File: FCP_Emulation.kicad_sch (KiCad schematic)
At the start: 115 parts, among them J1 Conn_01x10_Female, J2 Conn_01x10_Female, J3 Conn_01x10_Female, J4 Conn_01x02_Female, J5 Conn_01x02_Female, SW1 SW_DIP_x08, SW2 SW_DIP_x08, SW3 SW_DIP_x08, SW4 SW_DIP_x08, U1 LM2902, U2 LM2902, U3 LM2902, U4 LM2902, U5 LM2902, U6 LM2902, U7 LM2902, U8 LM2902

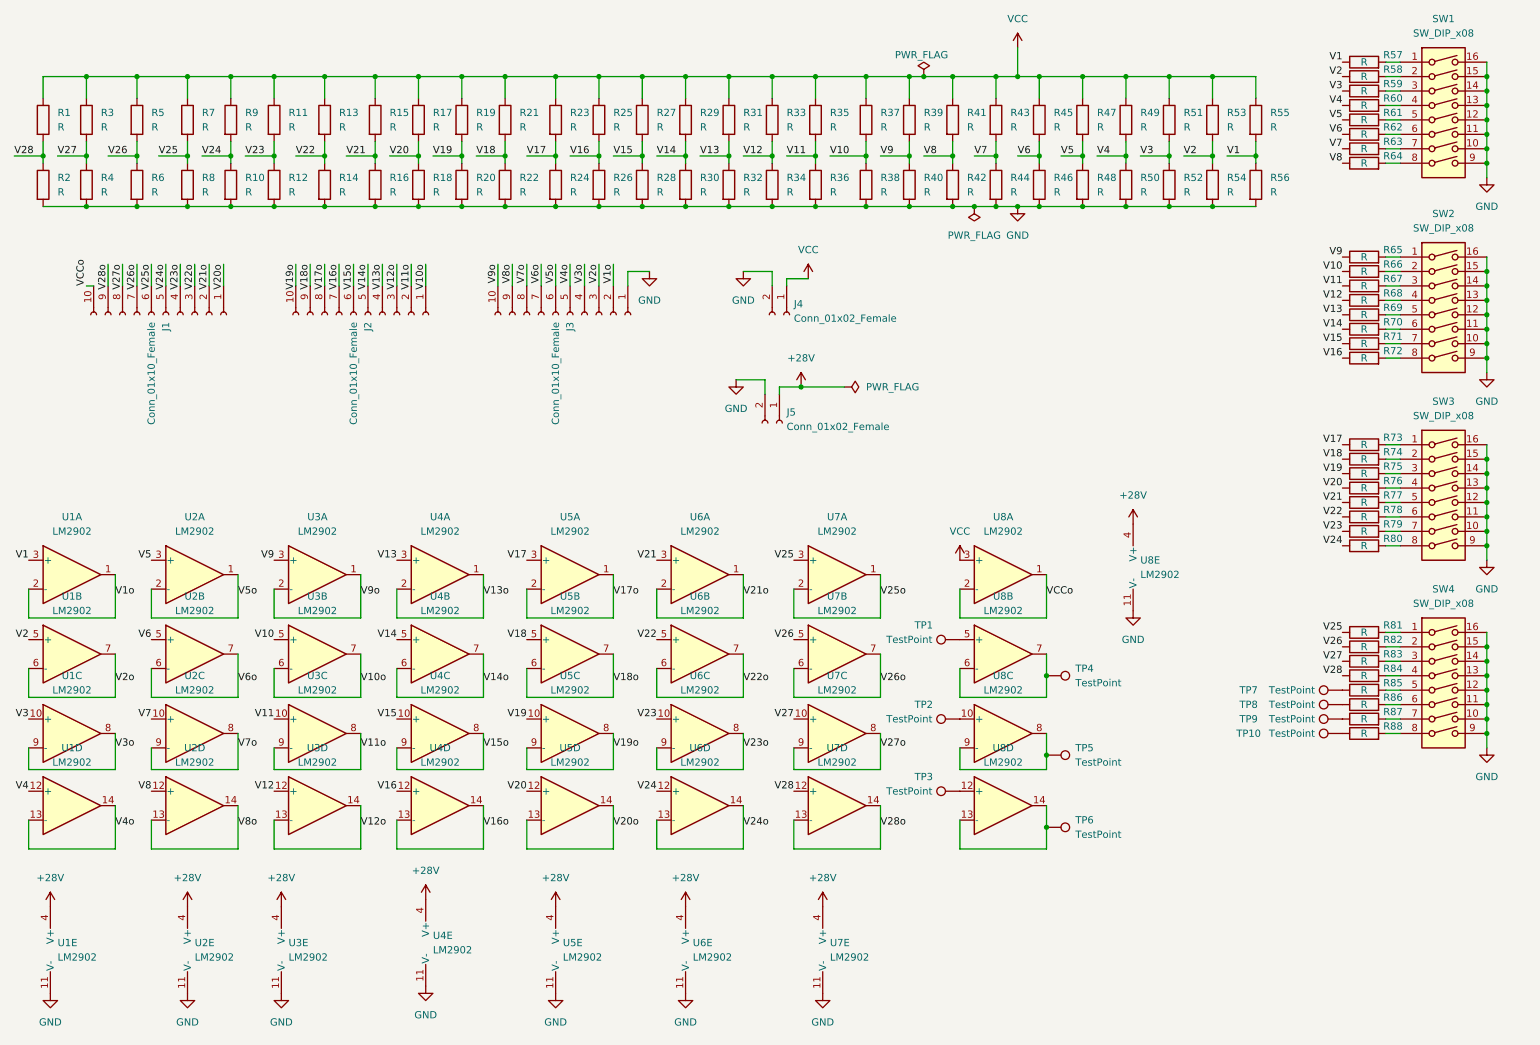
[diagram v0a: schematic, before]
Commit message: deleted a bunch of old stuff, added microcontroller, new op amp circuits
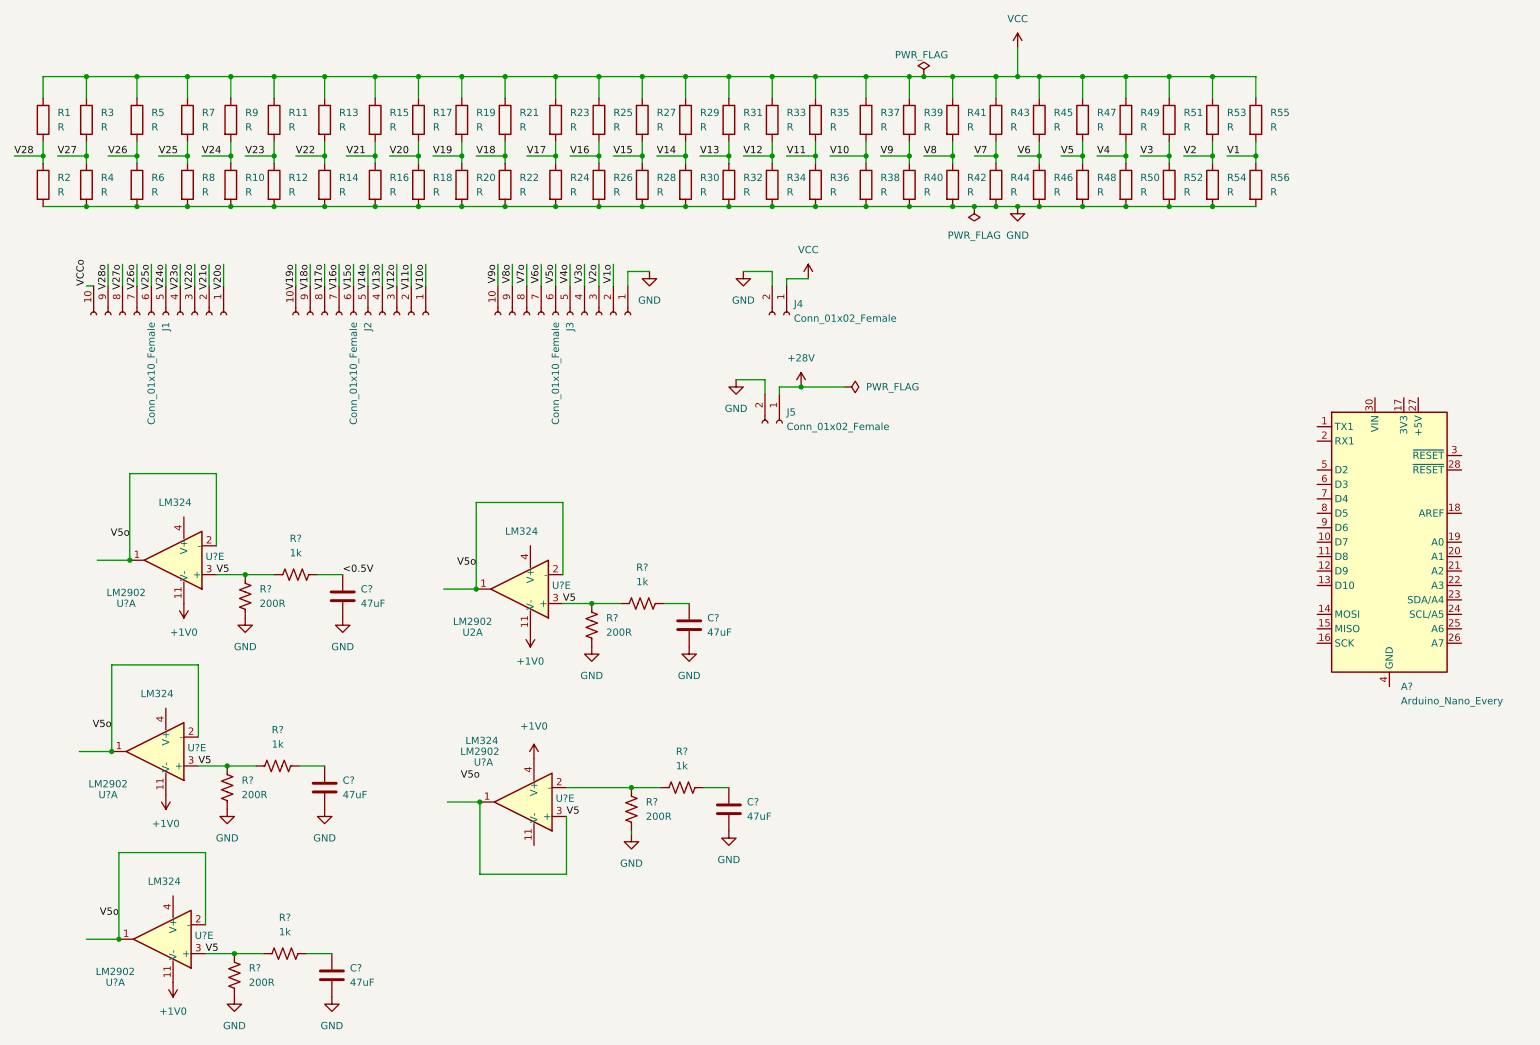
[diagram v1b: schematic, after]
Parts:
- removed R57, R58, R59, R60, R61, R62, R63, R64, R65, R66, R67, R68, R69, R70, R71, R72, R73, R74, R75, R76, R77, R78, R79, R80, R81, R82, R83, R84, R85, R86, R87, R88: R, Resistor_SMD:R_0805_2012Metric, symbol Device:R
- removed SW1, SW2, SW3, SW4: SW_DIP_x08, Package_DIP:DIP-16_W7.62mm, symbol Switch:SW_DIP_x08
- removed TP1, TP10, TP2, TP3, TP4, TP5, TP6, TP7, TP8, TP9: TestPoint, Connector_PinHeader_2.54mm:PinHeader_1x01_P2.54mm_Vertical, symbol Connector:TestPoint
- removed U1, U3, U4, U5, U6, U7, U8: LM2902, Package_SO:SO-14_3.9x8.65mm_P1.27mm, symbol Amplifier_Operational:LM2902
- removed unit 3 of U2
- removed unit 4 of U2
- removed unit 5 of U2
- removed unit 2 of U2
- added A?: Arduino_Nano_Every, Module:Arduino_Nano, symbol MCU_Module:Arduino_Nano_Every
- added C? (x5): 47uF, symbol Device:C
- added R? (x5): 200R, symbol Device:R_US
- added R? (x5): 1k, symbol Device:R_US
- added U? (x5): LM324, symbol Amplifier_Operational:LM324
- added U? (x4): LM2902, Package_SO:SO-14_3.9x8.65mm_P1.27mm, symbol Amplifier_Operational:LM2902
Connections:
- net GND: now also C?.2, C?.2, C?.2, C?.2, C?.2, R?.2, R?.2, R?.2, R?.2, R?.2
- net V5: now also R?.1, R?.1, R?.1, R?.1, R?.1, R?.1, R?.1, R?.1, U?.1, U?.3 (+), U?.3 (+), U?.3 (+), U?.3 (+)
- net V5o: now also U?.1, U?.1, U?.1, U?.2 (-), U?.2 (-), U?.2 (-)
- new net: C?.1, R?.2 (x4)
- new net: R?.1, R?.1, U?.2 (-)
- new net: A?.29 (GND), A?.4 (GND)
- new net +1V0: U?.11 (V-), U?.11 (V-), U?.11 (V-), U?.11 (V-), U?.4 (V+)
- new net <0.5V: C?.1, R?.2
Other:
- moved on the sheet: U2A

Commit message: created the op amp cases
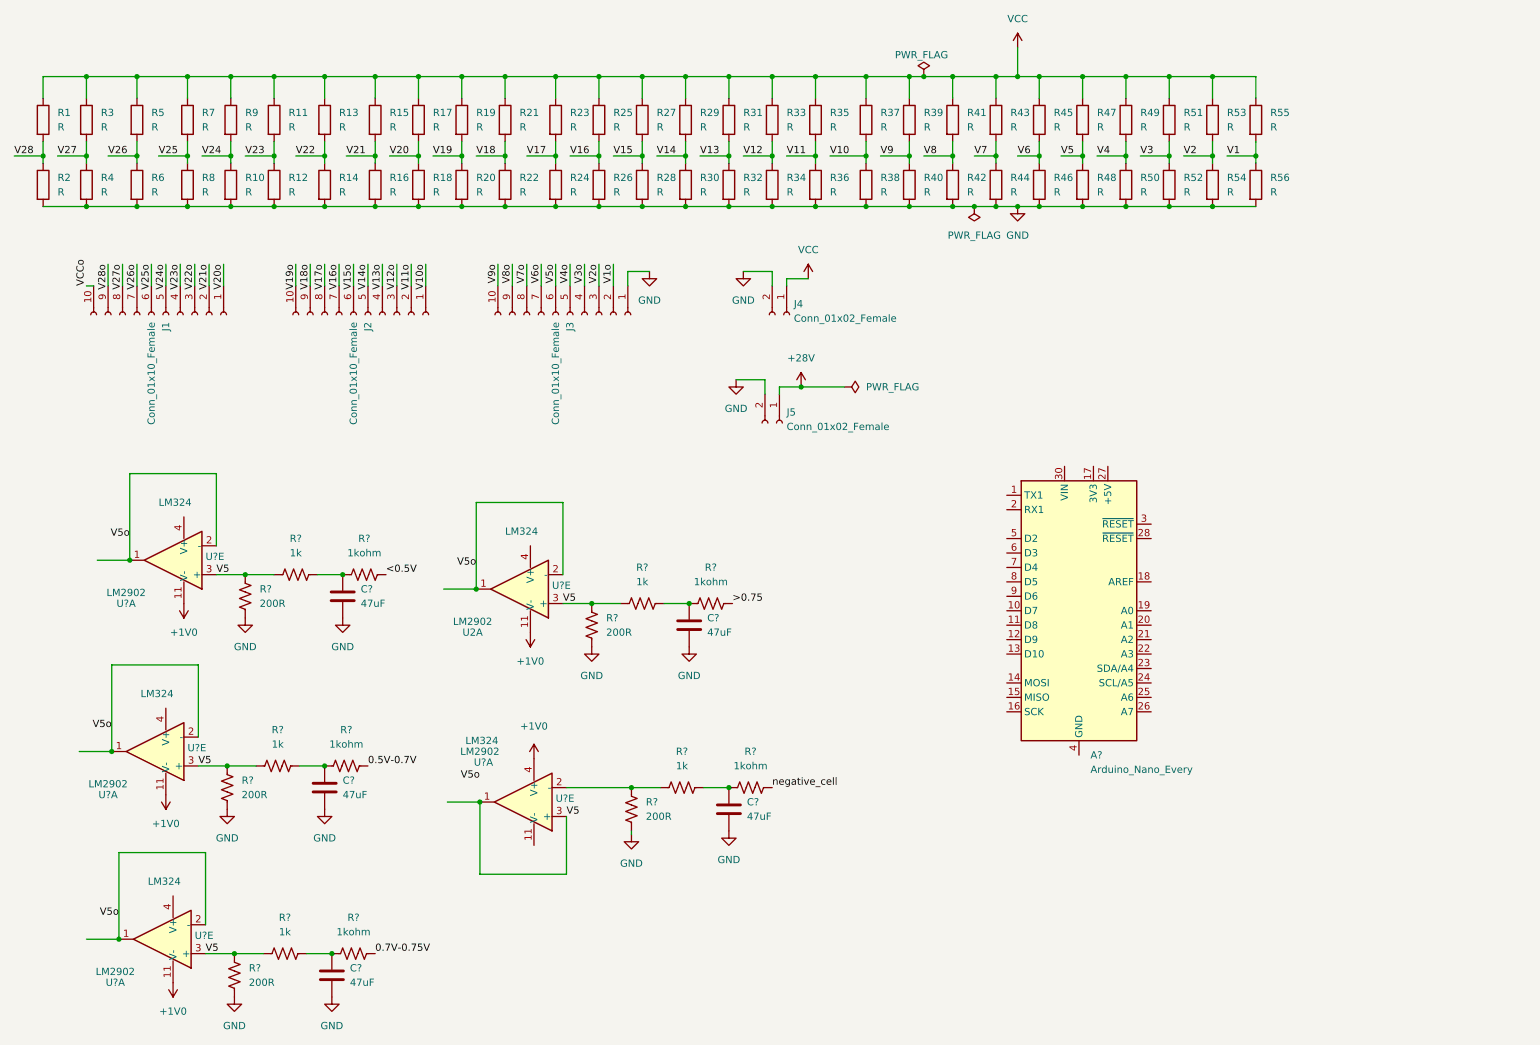
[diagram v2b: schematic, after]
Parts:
- added R? (x5): 1kohm, symbol Device:R_US
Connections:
- net <0.5V: now also R?.2; no longer C?.1, R?.2
- net at C?.1, R?.2: now also R?.1 (x4)
- new net: C?.1, R?.1, R?.2
- new net 0.5V-0.7V: R?.2
- new net 0.7V-0.75V: R?.2
- new net >0.75: R?.2
- new net negative_cell: R?.2
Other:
- moved on the sheet: A?
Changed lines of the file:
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@@
   (junction (at 201.93 50.8) (diameter 0) (color 0 0 0 0)
   )
+  (junction (at 69.85 182.245) (diameter 0) (color 0 0 0 0)
+  )
   (junction (at 59.69 50.8) (diameter 0) (color 0 0 0 0)
   )
@@
   (junction (at 44.45 41.91) (diameter 0) (color 0 0 0 0)
   )
+  (junction (at 71.755 115.57) (diameter 0) (color 0 0 0 0)
+  )
   (junction (at 154.94 27.94) (diameter 0) (color 0 0 0 0)
   )
@@
   (junction (at 132.08 41.91) (diameter 0) (color 0 0 0 0)
   )
+  (junction (at 132.715 120.65) (diameter 0) (color 0 0 0 0)
+  )
   (junction (at 124.46 50.8) (diameter 0) (color 0 0 0 0)
   )
   (junction (at 201.93 41.91) (diameter 0) (color 0 0 0 0)
   )
+  (junction (at 68.58 149.225) (diameter 0) (color 0 0 0 0)
+  )
   (junction (at 224.79 41.91) (diameter 0) (color 0 0 0 0)
   )
@@
   (junction (at 59.69 27.94) (diameter 0) (color 0 0 0 0)
   )
+  (junction (at 139.7 153.035) (diameter 0) (color 0 0 0 0)
+  )
   (junction (at 171.45 50.8) (diameter 0) (color 0 0 0 0)
   )
@@
     (effects (font (size 1.27 1.27)) (justify left bottom))
   )
-  (label "<0.5V" (at 71.755 115.57 0)
-    (effects (font (size 1.27 1.27)) (justify left bottom))
-  )
   (label "V5o" (at 31.115 142.875 180)
     (effects (font (size 1.27 1.27)) (justify right bottom))
   )
+  (label "<0.5V" (at 79.375 115.57 0)
+    (effects (font (size 1.27 1.27)) (justify left bottom))
+  )
   (label "V12" (at 142.24 41.91 0)
     (effects (font (size 1.27 1.27)) (justify left bottom))
@@
     (effects (font (size 1.27 1.27)) (justify right bottom))
   )
+  (label "negative_cell" (at 147.32 153.035 0)
+    (effects (font (size 1.27 1.27)) (justify left bottom))
+  )
   (label "V26o" (at 35.56 60.96 270)
     (effects (font (size 1.27 1.27)) (justify right bottom))
   )
+  (label ">0.75" (at 140.335 120.65 0)
+    (effects (font (size 1.27 1.27)) (justify left bottom))
+  )
   (label "V15" (at 119.38 41.91 0)
     (effects (font (size 1.27 1.27)) (justify left bottom))
@@
     (effects (font (size 1.27 1.27)) (justify left bottom))
   )
+  (label "0.5V-0.7V" (at 76.2 149.225 0)
+    (effects (font (size 1.27 1.27)) (justify left bottom))
+  )
   (label "V24" (at 46.99 41.91 0)
     (effects (font (size 1.27 1.27)) (justify left bottom))
@@
     (effects (font (size 1.27 1.27)) (justify left bottom))
   )
+  (label "0.7V-0.75V" (at 77.47 182.245 0)
+    (effects (font (size 1.27 1.27)) (justify left bottom))
+  )
   (label "V11" (at 149.86 41.91 0)
     (effects (font (size 1.27 1.27)) (justify left bottom))
@@
     (pin "2")
   )
+  (symbol (lib_id "Device:R_US") (at 136.525 120.65 90) (unit 1)
+    (in_bom yes) (on_board yes) (fields_autoplaced)
+    (property "Reference" "R?" (id 0) (at 136.525 114.3 90))
+    (property "Value" "1kohm" (id 1) (at 136.525 116.84 90))
+    (property "Footprint" "" (id 2) (at 136.779 119.634 90)
+      (effects (font (size 1.27 1.27)) hide)
+    )
+    (property "Datasheet" "~" (id 3) (at 136.525 120.65 0)
+      (effects (font (size 1.27 1.27)) hide)
+    )
+    (pin "1")
+    (pin "2")
+  )
   (symbol (lib_id "Device:R") (at 35.56 46.99 0) (unit 1)
     (in_bom yes) (on_board yes)
@@
     (pin "4")
   )
+  (symbol (lib_id "Device:R_US") (at 143.51 153.035 90) (unit 1)
+    (in_bom yes) (on_board yes) (fields_autoplaced)
+    (property "Reference" "R?" (id 0) (at 143.51 146.685 90))
+    (property "Value" "1kohm" (id 1) (at 143.51 149.225 90))
+    (property "Footprint" "" (id 2) (at 143.764 152.019 90)
+      (effects (font (size 1.27 1.27)) hide)
+    )
+    (property "Datasheet" "~" (id 3) (at 143.51 153.035 0)
+      (effects (font (size 1.27 1.27)) hide)
+    )
+    (pin "1")
+    (pin "2")
+  )
   (symbol (lib_id "power:VCC") (at 190.5 22.86 0) (unit 1)
     (in_bom yes) (on_board yes) (fields_autoplaced)
@@
     (pin "9")
   )
-  (symbol (lib_id "MCU_Module:Arduino_Nano_Every") (at 255.905 109.855 0) (unit 1)
+  (symbol (lib_id "MCU_Module:Arduino_Nano_Every") (at 201.295 121.92 0) (unit 1)
     (in_bom yes) (on_board yes) (fields_autoplaced)
-    (property "Reference" "A?" (id 0) (at 257.9244 135.255 0)
+    (property "Reference" "A?" (id 0) (at 203.3144 147.32 0)
       (effects (font (size 1.27 1.27)) (justify left))
     )
-    (property "Value" "Arduino_Nano_Every" (id 1) (at 257.9244 137.795 0)
+    (property "Value" "Arduino_Nano_Every" (id 1) (at 203.3144 149.86 0)
       (effects (font (size 1.27 1.27)) (justify left))
     )
-    (property "Footprint" "Module:Arduino_Nano" (id 2) (at 255.905 109.855 0)
+    (property "Footprint" "Module:Arduino_Nano" (id 2) (at 201.295 121.92 0)
       (effects (font (size 1.27 1.27) italic) hide)
     )
-    (property "Datasheet" "https://content.arduino.cc/assets/NANOEveryV3.0_sch.pdf" (id 3) (at 255.905 109.855 0)
+    (property "Datasheet" "https://content.arduino.cc/assets/NANOEveryV3.0_sch.pdf" (id 3) (at 201.295 121.92 0)
       (effects (font (size 1.27 1.27)) hide)
     )
@@
     (pin "2")
   )
+  (symbol (lib_id "Device:R_US") (at 75.565 115.57 90) (unit 1)
+    (in_bom yes) (on_board yes) (fields_autoplaced)
+    (property "Reference" "R?" (id 0) (at 75.565 109.22 90))
+    (property "Value" "1kohm" (id 1) (at 75.565 111.76 90))
+    (property "Footprint" "" (id 2) (at 75.819 114.554 90)
+      (effects (font (size 1.27 1.27)) hide)
+    )
+    (property "Datasheet" "~" (id 3) (at 75.565 115.57 0)
+      (effects (font (size 1.27 1.27)) hide)
+    )
+    (pin "1")
+    (pin "2")
+  )
   (symbol (lib_id "Device:R") (at 44.45 46.99 0) (unit 1)
     (in_bom yes) (on_board yes) (fields_autoplaced)
@@
     (pin "2")
   )
+  (symbol (lib_id "Device:R_US") (at 73.66 182.245 90) (unit 1)
+    (in_bom yes) (on_board yes) (fields_autoplaced)
+    (property "Reference" "R?" (id 0) (at 73.66 175.895 90))
+    (property "Value" "1kohm" (id 1) (at 73.66 178.435 90))
+    (property "Footprint" "" (id 2) (at 73.914 181.229 90)
+      (effects (font (size 1.27 1.27)) hide)
+    )
+    (property "Datasheet" "~" (id 3) (at 73.66 182.245 0)
+      (effects (font (size 1.27 1.27)) hide)
+    )
+    (pin "1")
+    (pin "2")
+  )
   (symbol (lib_id "Device:R") (at 77.47 35.56 0) (unit 1)
     (in_bom yes) (on_board yes) (fields_autoplaced)
@@
     (pin "2")
   )
+  (symbol (lib_id "Device:R_US") (at 72.39 149.225 90) (unit 1)
+    (in_bom yes) (on_board yes) (fields_autoplaced)
+    (property "Reference" "R?" (id 0) (at 72.39 142.875 90))
+    (property "Value" "1kohm" (id 1) (at 72.39 145.415 90))
+    (property "Footprint" "" (id 2) (at 72.644 148.209 90)
+      (effects (font (size 1.27 1.27)) hide)
+    )
+    (property "Datasheet" "~" (id 3) (at 72.39 149.225 0)
+      (effects (font (size 1.27 1.27)) hide)
+    )
+    (pin "1")
+    (pin "2")
+  )
   (symbol (lib_id "Device:R") (at 209.55 46.99 0) (unit 1)
     (in_bom yes) (on_board yes) (fields_autoplaced)
@@
       (reference "R56") (unit 1) (value "R") (footprint "Resistor_SMD:R_0805_2012Metric")
     )
+    (path "/0bec81f4-13e8-4507-92ff-04b394a826f0"
+      (reference "R?") (unit 1) (value "1kohm") (footprint "")
+    )
+    (path "/19d2e53f-44ea-4c54-b01e-c950a5b8b6cd"
+      (reference "R?") (unit 1) (value "1kohm") (footprint "")
+    )
     (path "/213c9ef1-4080-4bdb-90cf-90762afb3810"
       (reference "R?") (unit 1) (value "200R") (footprint "")
@@
       (reference "R?") (unit 1) (value "1k") (footprint "")
     )
+    (path "/7a3e2c43-a095-41e7-b0f4-82da1ee34d37"
+      (reference "R?") (unit 1) (value "1kohm") (footprint "")
+    )
     (path "/8962b89f-3088-47c8-a81e-22ebfa0190d6"
       (reference "R?") (unit 1) (value "200R") (footprint "")
     )
+    (path "/a46aff55-eb16-4686-9175-32adf769f71b"
+      (reference "R?") (unit 1) (value "1kohm") (footprint "")
+    )
+    (path "/b30a15db-0d46-41cc-85d6-30947b0b0e8d"
+      (reference "R?") (unit 1) (value "1kohm") (footprint "")
+    )
     (path "/da81b253-9021-4323-a20c-e9eba82fb6f9"
